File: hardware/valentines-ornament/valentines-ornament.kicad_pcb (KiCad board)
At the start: 2 copper layers, 21 parts, among them J1 AVR-ISP-6, SW1 SW_Push, U1 ATtiny85-20SU

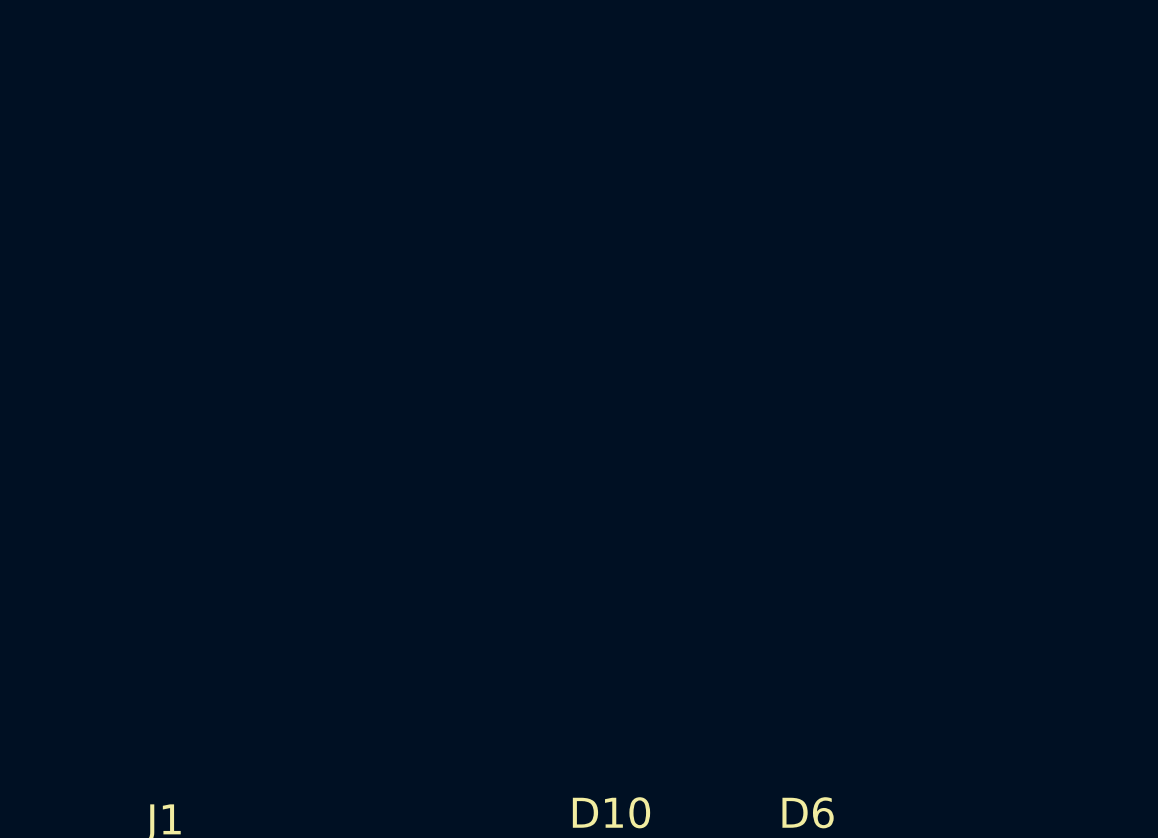
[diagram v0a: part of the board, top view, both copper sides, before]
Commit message: Add battery cell
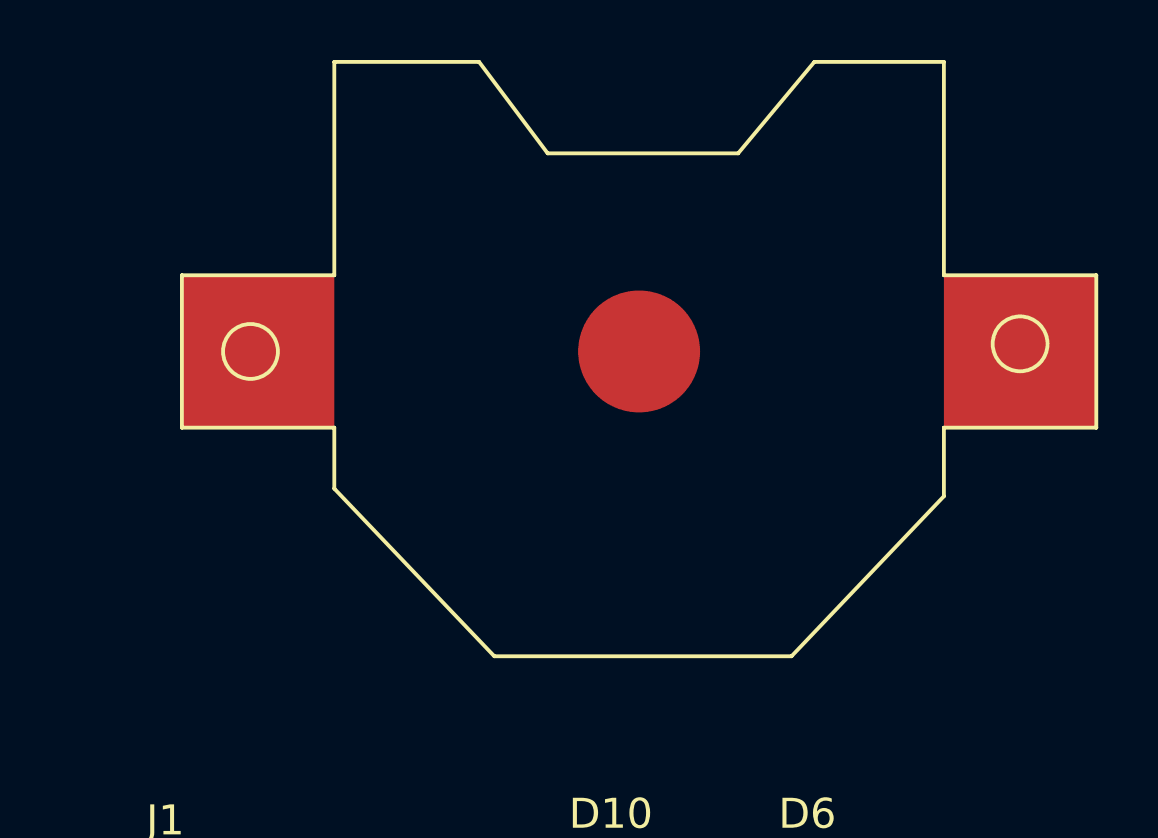
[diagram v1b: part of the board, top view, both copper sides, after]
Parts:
- added BT1: Battery_Cell, kicad-libs:CR2032-SMD, F.Cu at (149.6, 77.0)
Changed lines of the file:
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@@
     (tracks 0)
     (zones 0)
-    (modules 21)
+    (modules 22)
     (nets 13)
   )
@@
     (solder_mask_min_width 0.25)
     (aux_axis_origin 0 0)
-    (visible_elements FFFFFF7F)
+    (visible_elements 7FFFFFFF)
     (pcbplotparams
       (layerselection 0x010fc_ffffffff)
@@
       (net 2 GND))
   )
+  (module kicad-libs:CR2032-SMD (layer F.Cu)
+    (at 149.606 76.962)
+    (tags "battery cr2032 smt smd")
+    (fp_text reference BT1 (at -0.2032 -9.4615) (layer Eco1.User)
+      (effects (font (size 1.6764 1.6764) (thickness 0.13208)))
+    )
+    (fp_text value Battery_Cell (at 0.7112 13.18768) (layer Eco1.User)
+      (effects (font (size 1.6764 1.6764) (thickness 0.13208)))
+    )
+    (fp_line (start -15.24 2.54) (end -10.16 2.54) (layer F.SilkS) (width 0.127))
+    (fp_line (start -10.16 2.54) (end -10.16 4.572) (layer F.SilkS) (width 0.127))
+    (fp_line (start -10.16 4.572) (end -4.826 10.16) (layer F.SilkS) (width 0.127))
+    (fp_line (start -4.826 10.16) (end 5.08 10.16) (layer F.SilkS) (width 0.127))
+    (fp_line (start 5.08 10.16) (end 10.16 4.826) (layer F.SilkS) (width 0.127))
+    (fp_line (start 10.16 4.826) (end 10.16 2.54) (layer F.SilkS) (width 0.127))
+    (fp_line (start 10.16 2.54) (end 15.24 2.54) (layer F.SilkS) (width 0.127))
+    (fp_line (start 15.24 2.54) (end 15.24 -2.54) (layer F.SilkS) (width 0.127))
+    (fp_line (start 15.24 -2.54) (end 10.16 -2.54) (layer F.SilkS) (width 0.127))
+    (fp_line (start 10.16 -2.54) (end 10.16 -9.652) (layer F.SilkS) (width 0.127))
+    (fp_line (start 10.16 -9.652) (end 5.842 -9.652) (layer F.SilkS) (width 0.127))
+    (fp_line (start 5.842 -9.652) (end 3.302 -6.604) (layer F.SilkS) (width 0.127))
+    (fp_line (start 3.302 -6.604) (end -3.048 -6.604) (layer F.SilkS) (width 0.127))
+    (fp_line (start -3.048 -6.604) (end -5.334 -9.652) (layer F.SilkS) (width 0.127))
+    (fp_line (start -5.334 -9.652) (end -10.16 -9.652) (layer F.SilkS) (width 0.127))
+    (fp_line (start -10.16 -9.652) (end -10.16 -2.54) (layer F.SilkS) (width 0.127))
+    (fp_line (start -10.16 -2.54) (end -15.24 -2.54) (layer F.SilkS) (width 0.127))
+    (fp_line (start -15.24 -2.54) (end -15.24 2.54) (layer F.SilkS) (width 0.127))
+    (fp_arc (start 0 0) (end -8.99922 0) (angle -90) (layer F.Mask) (width 0.127))
+    (fp_arc (start 0 0) (end 0 -8.99922) (angle -90) (layer F.Mask) (width 0.127))
+    (fp_arc (start 0 0) (end 8.99922 0) (angle -90) (layer F.Mask) (width 0.127))
+    (fp_arc (start 0 0) (end 0 8.99922) (angle -90) (layer F.Mask) (width 0.127))
+    (fp_circle (center -12.954 0) (end -12.0396 0) (layer F.SilkS) (width 0.127))
+    (fp_circle (center 12.7 -0.254) (end 13.6144 -0.254) (layer F.SilkS) (width 0.127))
+    (pad 2 smd circle (at 0 0) (size 4.064 4.064) (layers F.Cu F.Paste F.Mask)
+      (net 2 GND))
+    (pad 1 smd rect (at -12.7 0) (size 5.08 5.08) (layers F.Cu F.Paste F.Mask)
+      (net 1 +3V3))
+    (pad 1 smd rect (at 12.7 0) (size 5.08 5.08) (layers F.Cu F.Paste F.Mask)
+      (net 1 +3V3))
+  )
 )

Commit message: Add heart solder mask logo, switch resistors to 0805
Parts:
- added G1: mask-symbol, kicad-libs:abstract-heart, F.Cu at (104.9, 67.3)
- R1, R2, R3, R4, R5: footprint Resistors_SMD:R_1206_HandSoldering -> Resistors_SMD:R_0805_HandSoldering
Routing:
- added copper zone on F.Cu, net (none)
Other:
- board outline added: 47.4 x 48 mm

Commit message: Position all the parts
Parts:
- BT1, C1, J1, R1, R2, R3, R4, R5, SW1, U1: moved to B.Cu
- moved R5 73.4 mm to (92.5, 66.8)
- moved R2 67.1 mm to (104.9, 54.4)
- moved R1 65.2 mm to (104.9, 57.9)
- moved R3 64.7 mm to (118.1, 49.9), turned to 180 degrees
- moved C1 63.9 mm to (110.7, 49.6), turned to 270 degrees
- moved D12 62.8 mm to (113.8, 52.9), turned to 90 degrees
- moved D11 61.3 mm to (107.2, 58.8), turned to 315 degrees
- moved D4 61.2 mm to (90.5, 70.6), turned to 345 degrees
- moved R4 57.9 mm to (122.4, 57.3), turned to 180 degrees
- moved SW1 52.6 mm to (92.1, 72.3)
- moved D6 52.6 mm to (106.9, 73.5), turned to 130 degrees
- moved D5 52.1 mm to (98.6, 76.2), turned to 335 degrees
- moved U1 50.2 mm to (113.5, 56.6), turned to 270 degrees
- moved D1 47.5 mm to (91.7, 83.0), turned to 90 degrees
- moved D8 47.0 mm to (114.7, 70.3), turned to 270 degrees
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
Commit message: Tweak layout
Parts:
- moved D5 0.89 mm to (98.7, 77.1), turned to 315 degrees
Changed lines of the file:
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@@
   (layers
     (0 F.Cu signal)
-    (31 B.Cu signal hide)
+    (31 B.Cu signal)
     (32 B.Adhes user)
     (33 F.Adhes user)
-    (34 B.Paste user hide)
+    (34 B.Paste user)
     (35 F.Paste user)
     (36 B.SilkS user)
     (37 F.SilkS user)
-    (38 B.Mask user hide)
+    (38 B.Mask user)
     (39 F.Mask user)
     (40 Dwgs.User user)
@@
     (tags "LED 1206")
     (attr smd)
-    (fp_text reference D1 (at 0 -1.85 90) (layer F.SilkS)
+    (fp_text reference D1 (at 0.095 0.127 90) (layer F.SilkS)
       (effects (font (size 1 1) (thickness 0.15)))
     )
@@
     (tags "LED 1206")
     (attr smd)
-    (fp_text reference D2 (at 0 -1.85 250) (layer F.SilkS)
+    (fp_text reference D2 (at 0.075904 -0.162778 250) (layer F.SilkS)
       (effects (font (size 1 1) (thickness 0.15)))
     )
@@
     (tags "LED 1206")
     (attr smd)
-    (fp_text reference D3 (at 0 -1.85 170) (layer F.SilkS)
+    (fp_text reference D3 (at 0.093557 -0.016497 170) (layer F.SilkS)
       (effects (font (size 1 1) (thickness 0.15)))
     )
@@
     (tags "LED 1206")
     (attr smd)
-    (fp_text reference D4 (at 0 -1.85 345) (layer F.SilkS)
+    (fp_text reference D4 (at 0.00196 0.130955 345) (layer F.SilkS)
       (effects (font (size 1 1) (thickness 0.15)))
     )
@@
   )
   (module LEDs:LED_1206_HandSoldering (layer F.Cu)
-    (at 98.584 76.2 335)
-    (descr "LED SMD 1206, hand soldering")
-    (tags "LED 1206")
-    (attr smd)
-    (fp_text reference D5 (at 0 -1.85 335) (layer F.SilkS)
-      (effects (font (size 1 1) (thickness 0.15)))
-    )
-    (fp_text value LED (at 0 1.9 335) (layer F.Fab)
-      (effects (font (size 1 1) (thickness 0.15)))
-    )
-    (fp_line (start -3.1 -0.95) (end -3.1 0.95) (layer F.SilkS) (width 0.12))
-    (fp_line (start -0.4 0) (end 0.2 -0.4) (layer F.Fab) (width 0.1))
-    (fp_line (start 0.2 -0.4) (end 0.2 0.4) (layer F.Fab) (width 0.1))
-    (fp_line (start 0.2 0.4) (end -0.4 0) (layer F.Fab) (width 0.1))
-    (fp_line (start -0.45 -0.4) (end -0.45 0.4) (layer F.Fab) (width 0.1))
-    (fp_line (start -1.6 0.8) (end -1.6 -0.8) (layer F.Fab) (width 0.1))
-    (fp_line (start 1.6 0.8) (end -1.6 0.8) (layer F.Fab) (width 0.1))
-    (fp_line (start 1.6 -0.8) (end 1.6 0.8) (layer F.Fab) (width 0.1))
-    (fp_line (start -1.6 -0.8) (end 1.6 -0.8) (layer F.Fab) (width 0.1))
-    (fp_line (start -3.1 0.95) (end 1.6 0.95) (layer F.SilkS) (width 0.12))
-    (fp_line (start -3.1 -0.95) (end 1.6 -0.95) (layer F.SilkS) (width 0.12))
-    (fp_line (start -3.25 -1.11) (end 3.25 -1.11) (layer F.CrtYd) (width 0.05))
-    (fp_line (start -3.25 -1.11) (end -3.25 1.1) (layer F.CrtYd) (width 0.05))
-    (fp_line (start 3.25 1.1) (end 3.25 -1.11) (layer F.CrtYd) (width 0.05))
-    (fp_line (start 3.25 1.1) (end -3.25 1.1) (layer F.CrtYd) (width 0.05))
-    (pad 1 smd rect (at -2 0 335) (size 2 1.7) (layers F.Cu F.Paste F.Mask)
+    (at 98.679 77.089 315)
+    (descr "LED SMD 1206, hand soldering")
+    (tags "LED 1206")
+    (attr smd)
+    (fp_text reference D5 (at -0.089803 0.089803 315) (layer F.SilkS)
+      (effects (font (size 1 1) (thickness 0.15)))
+    )
+    (fp_text value LED (at 0 1.9 315) (layer F.Fab)
+      (effects (font (size 1 1) (thickness 0.15)))
+    )
+    (fp_line (start -3.1 -0.95) (end -3.1 0.95) (layer F.SilkS) (width 0.12))
+    (fp_line (start -0.4 0) (end 0.2 -0.4) (layer F.Fab) (width 0.1))
+    (fp_line (start 0.2 -0.4) (end 0.2 0.4) (layer F.Fab) (width 0.1))
+    (fp_line (start 0.2 0.4) (end -0.4 0) (layer F.Fab) (width 0.1))
+    (fp_line (start -0.45 -0.4) (end -0.45 0.4) (layer F.Fab) (width 0.1))
+    (fp_line (start -1.6 0.8) (end -1.6 -0.8) (layer F.Fab) (width 0.1))
+    (fp_line (start 1.6 0.8) (end -1.6 0.8) (layer F.Fab) (width 0.1))
+    (fp_line (start 1.6 -0.8) (end 1.6 0.8) (layer F.Fab) (width 0.1))
+    (fp_line (start -1.6 -0.8) (end 1.6 -0.8) (layer F.Fab) (width 0.1))
+    (fp_line (start -3.1 0.95) (end 1.6 0.95) (layer F.SilkS) (width 0.12))
+    (fp_line (start -3.1 -0.95) (end 1.6 -0.95) (layer F.SilkS) (width 0.12))
+    (fp_line (start -3.25 -1.11) (end 3.25 -1.11) (layer F.CrtYd) (width 0.05))
+    (fp_line (start -3.25 -1.11) (end -3.25 1.1) (layer F.CrtYd) (width 0.05))
+    (fp_line (start 3.25 1.1) (end 3.25 -1.11) (layer F.CrtYd) (width 0.05))
+    (fp_line (start 3.25 1.1) (end -3.25 1.1) (layer F.CrtYd) (width 0.05))
+    (pad 1 smd rect (at -2 0 315) (size 2 1.7) (layers F.Cu F.Paste F.Mask)
       (net 6 "Net-(D10-Pad2)"))
-    (pad 2 smd rect (at 2 0 335) (size 2 1.7) (layers F.Cu F.Paste F.Mask)
+    (pad 2 smd rect (at 2 0 315) (size 2 1.7) (layers F.Cu F.Paste F.Mask)
       (net 5 "Net-(D3-Pad1)"))
     (model ${KISYS3DMOD}/LEDs.3dshapes/LED_1206.wrl
@@
     (tags "LED 1206")
     (attr smd)
-    (fp_text reference D6 (at 0 -1.85 130) (layer F.SilkS)
+    (fp_text reference D6 (at -0.117857 -0.057121 130) (layer F.SilkS)
       (effects (font (size 1 1) (thickness 0.15)))
     )
@@
     (tags "LED 1206")
     (attr smd)
-    (fp_text reference D7 (at 0 -1.85 35) (layer F.SilkS)
+    (fp_text reference D7 (at -0.046631 0.122387 35) (layer F.SilkS)
       (effects (font (size 1 1) (thickness 0.15)))
     )
@@
     (tags "LED 1206")
     (attr smd)
-    (fp_text reference D8 (at 0 -1.85 270) (layer F.SilkS)
+    (fp_text reference D8 (at 0.095 -0.127 270) (layer F.SilkS)
       (effects (font (size 1 1) (thickness 0.15)))
     )
@@
     (tags "LED 1206")
     (attr smd)
-    (fp_text reference D9 (at 0 -1.85 330) (layer F.SilkS)
+    (fp_text reference D9 (at 0.035787 0.125985 330) (layer F.SilkS)
       (effects (font (size 1 1) (thickness 0.15)))
     )
@@
     (tags "LED 1206")
     (attr smd)
-    (fp_text reference D10 (at 0 -1.85 335) (layer F.SilkS)
-      (effects (font (size 1 1) (thickness 0.15)))
+    (fp_text reference D10 (at 0.086099 -0.040149 335) (layer F.SilkS)
+      (effects (font (size 0.8 0.8) (thickness 0.15)))
     )
     (fp_text value LED (at 0 1.9 335) (layer F.Fab)
@@
     (tags "LED 1206")
     (attr smd)
-    (fp_text reference D11 (at 0 -1.85 315) (layer F.SilkS)
-      (effects (font (size 1 1) (thickness 0.15)))
+    (fp_text reference D11 (at 0.156978 0.022627 315) (layer F.SilkS)
+      (effects (font (size 0.8 0.8) (thickness 0.15)))
     )
     (fp_text value LED (at 0 1.9 315) (layer F.Fab)
@@
     (tags "LED 1206")
     (attr smd)
-    (fp_text reference D12 (at 0 -1.85 90) (layer F.SilkS)
-      (effects (font (size 1 1) (thickness 0.15)))
+    (fp_text reference D12 (at 0.095 0 90) (layer F.SilkS)
+      (effects (font (size 0.8 0.8) (thickness 0.1)))
     )
     (fp_text value LED (at 0 1.9 90) (layer F.Fab)

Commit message: Finish placing
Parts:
- added H1: MountingHole, Mounting_Holes:MountingHole_2.2mm_M2, F.Cu at (125.1, 87.5)
- added H2: MountingHole, Mounting_Holes:MountingHole_2.2mm_M2, F.Cu at (104.5, 66.3)
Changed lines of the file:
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@@
     (tracks 0)
     (zones 0)
-    (modules 23)
+    (modules 25)
     (nets 13)
   )
@@
     (fp_line (start 3.25 1.1) (end 3.25 -1.11) (layer F.CrtYd) (width 0.05))
     (fp_line (start 3.25 1.1) (end -3.25 1.1) (layer F.CrtYd) (width 0.05))
-    (pad 1 smd rect (at -2 0 315) (size 2 1.7) (layers F.Cu F.Paste F.Mask)
+    (pad 1 smd rect (at -2.000001 0 315) (size 2 1.7) (layers F.Cu F.Paste F.Mask)
       (net 6 "Net-(D10-Pad2)"))
-    (pad 2 smd rect (at 2 0 315) (size 2 1.7) (layers F.Cu F.Paste F.Mask)
+    (pad 2 smd rect (at 2.000001 0 315) (size 2 1.7) (layers F.Cu F.Paste F.Mask)
       (net 5 "Net-(D3-Pad1)"))
     (model ${KISYS3DMOD}/LEDs.3dshapes/LED_1206.wrl
@@
     (fp_line (start -0.4 0) (end 0.2 -0.4) (layer F.Fab) (width 0.1))
     (fp_line (start -3.1 -0.95) (end -3.1 0.95) (layer F.SilkS) (width 0.12))
-    (pad 2 smd rect (at 2 0 335) (size 2 1.7) (layers F.Cu F.Paste F.Mask)
+    (pad 2 smd rect (at 2.000001 0 335) (size 2 1.7) (layers F.Cu F.Paste F.Mask)
       (net 6 "Net-(D10-Pad2)"))
-    (pad 1 smd rect (at -2 0 335) (size 2 1.7) (layers F.Cu F.Paste F.Mask)
+    (pad 1 smd rect (at -2.000001 0 335) (size 2 1.7) (layers F.Cu F.Paste F.Mask)
       (net 3 "Net-(D1-Pad1)"))
     (model ${KISYS3DMOD}/LEDs.3dshapes/LED_1206.wrl
@@
     (fp_line (start 3.25 1.1) (end 3.25 -1.11) (layer F.CrtYd) (width 0.05))
     (fp_line (start 3.25 1.1) (end -3.25 1.1) (layer F.CrtYd) (width 0.05))
-    (pad 1 smd rect (at -2 0 315) (size 2 1.7) (layers F.Cu F.Paste F.Mask)
+    (pad 1 smd rect (at -2.000001 0 315) (size 2 1.7) (layers F.Cu F.Paste F.Mask)
       (net 6 "Net-(D10-Pad2)"))
-    (pad 2 smd rect (at 2 0 315) (size 2 1.7) (layers F.Cu F.Paste F.Mask)
+    (pad 2 smd rect (at 2.000001 0 315) (size 2 1.7) (layers F.Cu F.Paste F.Mask)
       (net 4 "Net-(D1-Pad2)"))
     (model ${KISYS3DMOD}/LEDs.3dshapes/LED_1206.wrl
@@
     )
   )
+  (module Mounting_Holes:MountingHole_2.2mm_M2 (layer F.Cu)
+    (at 125.095 87.503)
+    (descr "Mounting Hole 2.2mm, no annular, M2")
+    (tags "mounting hole 2.2mm no annular m2")
+    (attr virtual)
+    (fp_text reference H1 (at 0 -3.2) (layer F.SilkS)
+      (effects (font (size 1 1) (thickness 0.15)))
+    )
+    (fp_text value MountingHole (at 0 3.2) (layer F.Fab)
+      (effects (font (size 1 1) (thickness 0.15)))
+    )
+    (fp_text user %R (at 0.3 0) (layer F.Fab)
+      (effects (font (size 1 1) (thickness 0.15)))
+    )
+    (fp_circle (center 0 0) (end 2.2 0) (layer Cmts.User) (width 0.15))
+    (fp_circle (center 0 0) (end 2.45 0) (layer F.CrtYd) (width 0.05))
+    (pad 1 np_thru_hole circle (at 0 0) (size 2.2 2.2) (drill 2.2) (layers *.Cu *.Mask))
+  )
+  (module Mounting_Holes:MountingHole_2.2mm_M2 (layer F.Cu)
+    (at 104.521 66.294)
+    (descr "Mounting Hole 2.2mm, no annular, M2")
+    (tags "mounting hole 2.2mm no annular m2")
+    (attr virtual)
+    (fp_text reference H2 (at 0 -3.2) (layer F.SilkS)
+      (effects (font (size 1 1) (thickness 0.15)))
+    )
+    (fp_text value MountingHole (at 0 3.2) (layer F.Fab)
+      (effects (font (size 1 1) (thickness 0.15)))
+    )
+    (fp_circle (center 0 0) (end 2.45 0) (layer F.CrtYd) (width 0.05))
+    (fp_circle (center 0 0) (end 2.2 0) (layer Cmts.User) (width 0.15))
+    (fp_text user %R (at 0.3 0) (layer F.Fab)
+      (effects (font (size 1 1) (thickness 0.15)))
+    )
+    (pad 1 np_thru_hole circle (at 0 0) (size 2.2 2.2) (drill 2.2) (layers *.Cu *.Mask))
+  )
   (gr_line (start 128.651 64.262) (end 128.651 65.405) (layer Edge.Cuts) (width 0.2))

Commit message: Finished routing
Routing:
- net Net-(D1-Pad1): track 0.00 -> 113.8 mm, vias 0 -> 5
- net Net-(D1-Pad2): track 0.00 -> 98.3 mm, vias 0 -> 3
- net Net-(D3-Pad1): track 0.00 -> 81.4 mm, vias 0 -> 1
- net +3V3: track 0.00 -> 76.4 mm, vias 0 -> 2
- net Net-(D10-Pad2): track 0.00 -> 69.8 mm, vias 0 -> 8
- net /SCK_BUTTON: track 0.00 -> 54.4 mm
- net GND: track 0.00 -> 22.0 mm
- net /MOSI: track 0.00 -> 21.6 mm, vias 0 -> 2
- net /MISO: track 0.00 -> 20.1 mm
- net /RST: track 0.00 -> 10.7 mm, vias 0 -> 2
- net Net-(R3-Pad2): track 0.00 -> 7.77 mm
- net Net-(R4-Pad2): track 0.00 -> 4.79 mm
- added copper zone on B.Cu, net GND
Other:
- net class Default: clearance 0.2 -> 0.1524; trace_width 0.25 -> 0.1524; via_dia 0.8 -> 0.6858; via_drill 0.4 -> 0.3302
- net class VCC added: clearance 0.1524, trace_width 0.3048, via_dia 1.27, via_drill 0.6604
- rule pad_to_mask_clearance: 0.051 -> 0.0508
- rule trace_clearance: 0.2 -> 0.1524
- rule trace_min: 0.2 -> 0.1524
- rule via_min_drill: 0.3 -> 0.3302
- rule via_min_size: 0.4 -> 0.508

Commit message: Add some text
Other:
- board text added: "Bonnie, From my heart, to yours,"
- board text added: "Happy Valentines Day! I love you! Peter"
- board text added: "You light up my heart, my love."
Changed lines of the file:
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@@
   (general
     (thickness 1.6)
-    (drawings 37)
+    (drawings 40)
     (tracks 272)
     (zones 0)
@@
   (page A4)
   (layers
-    (0 F.Cu signal)
+    (0 F.Cu signal hide)
     (31 B.Cu signal)
     (32 B.Adhes user)
-    (33 F.Adhes user)
+    (33 F.Adhes user hide)
     (34 B.Paste user)
-    (35 F.Paste user)
+    (35 F.Paste user hide)
     (36 B.SilkS user)
-    (37 F.SilkS user)
+    (37 F.SilkS user hide)
     (38 B.Mask user)
-    (39 F.Mask user)
+    (39 F.Mask user hide)
     (40 Dwgs.User user)
     (41 Cmts.User user)
@@
     (pad 1 np_thru_hole circle (at 0 0) (size 2.2 2.2) (drill 2.2) (layers *.Cu *.Mask))
   )
+  (gr_text "You light up my heart, \nmy love." (at 103.505 64.008 45) (layer B.SilkS)
+    (effects (font (size 1 1) (thickness 0.25)))
+  )
+  (gr_text "Bonnie,\nFrom my heart,\nto yours," (at 91.821 80.518 45) (layer B.SilkS)
+    (effects (font (size 1.2 1.2) (thickness 0.3)))
+  )
+  (gr_text "Happy \nValentines Day!\nI love you!\nPeter" (at 123.063 66.167 45) (layer B.SilkS)
+    (effects (font (size 1.2 1.2) (thickness 0.3)))
+  )
   (gr_line (start 128.651 64.262) (end 128.651 65.405) (layer Edge.Cuts) (width 0.2))
